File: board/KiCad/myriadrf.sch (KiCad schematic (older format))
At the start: 1 part, among them J1 FX10B_80S_8

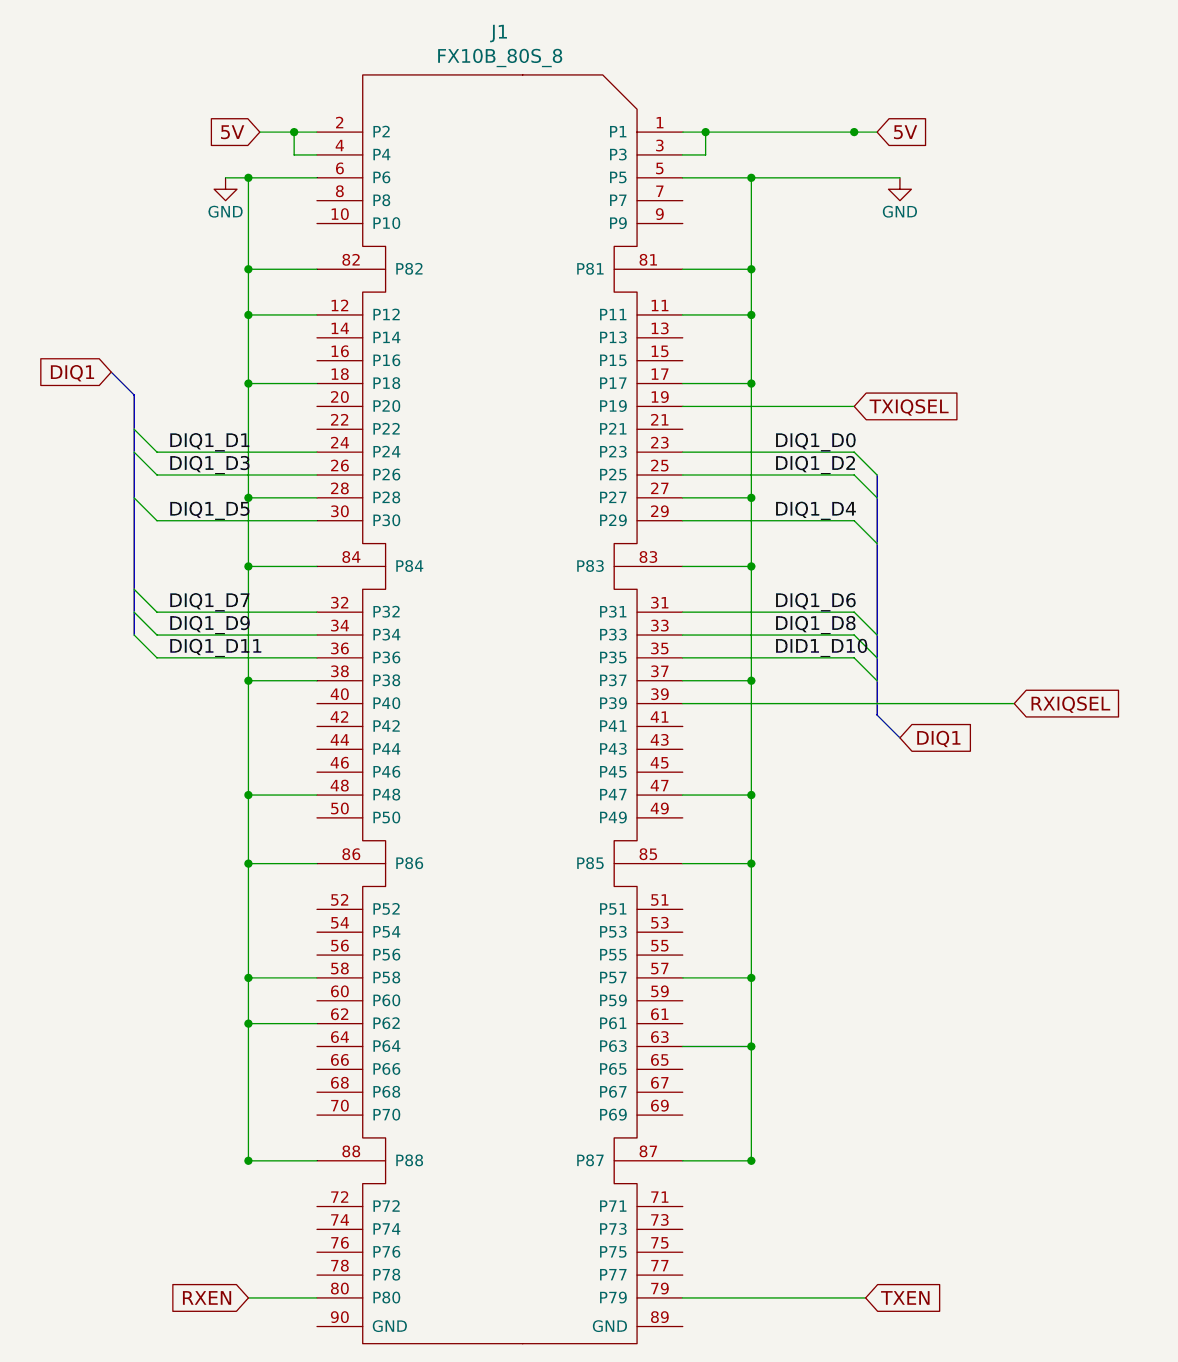
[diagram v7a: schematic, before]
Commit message: DIQ2 Bus added
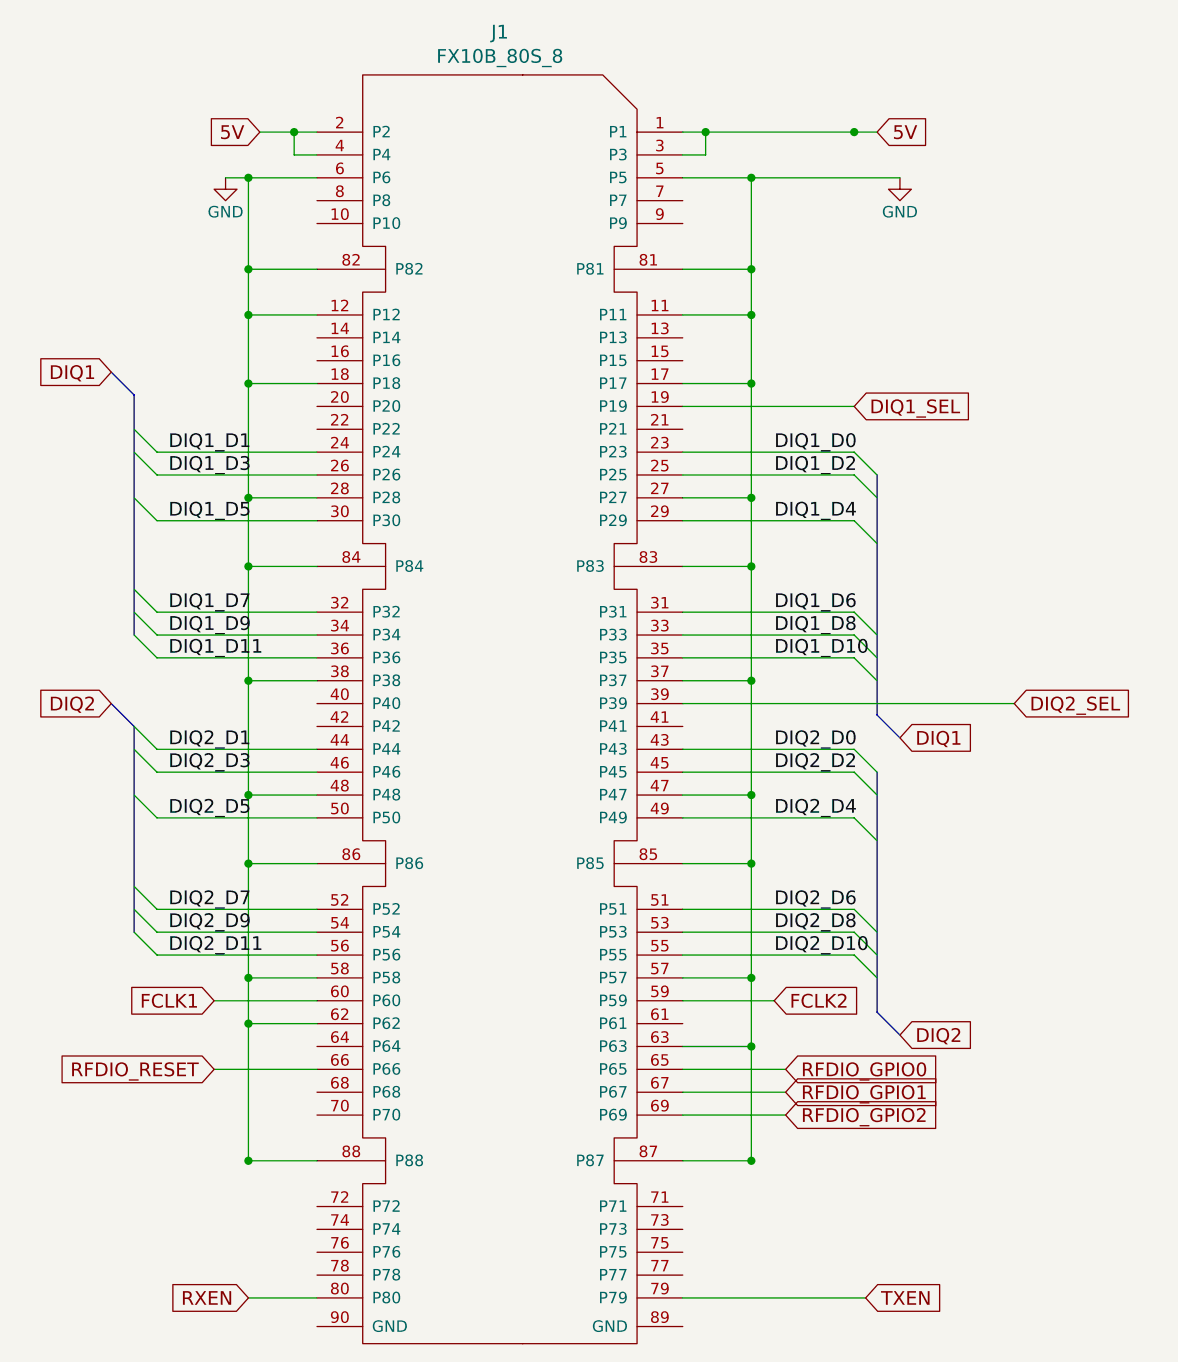
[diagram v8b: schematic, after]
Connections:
- net DIQ2_D0: now reaches J1.43 (P43)
- net DIQ2_D1: now reaches J1.44 (P44)
- net DIQ2_D2: now reaches J1.45 (P45)
- net DIQ2_D3: now reaches J1.46 (P46)
- net DIQ2_D4: now reaches J1.49 (P49)
- net DIQ2_D5: now reaches J1.50 (P50)
- net DIQ2_D6: now reaches J1.51 (P51)
- net DIQ2_D7: now reaches J1.52 (P52)
- net DIQ2_D8: now reaches J1.53 (P53)
- net DIQ2_D9: now reaches J1.54 (P54)
- net DIQ2_D10: now reaches J1.55 (P55)
- net DIQ2_D11: now reaches J1.56 (P56)
- net FCLK2: now reaches J1.59 (P59)
- net FCLK1: now reaches J1.60 (P60)
- net RFDIO_GPIO0: now reaches J1.65 (P65)
- net RFDIO_RESET: now reaches J1.66 (P66)
- net RFDIO_GPIO1: now reaches J1.67 (P67)
- net RFDIO_GPIO2: now reaches J1.69 (P69)
- net DID1_D10 renamed DIQ1_D10
- net RXIQSEL renamed DIQ2_SEL
- net TXIQSEL renamed DIQ1_SEL
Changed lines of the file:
@@
 DIQ1_D8
 Text Label 6800 3550 0    60   ~ 0
-DID1_D10
+DIQ1_D10
 Text Label 4150 2650 0    60   ~ 0
 DIQ1_D1
@@
 	6400 2450 7150 2450
 Text GLabel 7150 2450 2    60   Input ~ 0
-TXIQSEL
+DIQ1_SEL
 Wire Wire Line
 	6400 3750 7850 3750
 Text GLabel 7850 3750 2    60   Input ~ 0
-RXIQSEL
+DIQ2_SEL
 Wire Wire Line
 	4500 5750 4500 1450
@@
 Text GLabel 7200 6350 2    60   Input ~ 0
 TXEN
+Wire Bus Line
+	7250 4050 7250 5100
+Wire Wire Line
+	6400 3950 7150 3950
+Entry Wire Line
+	7150 3950 7250 4050
+Entry Wire Line
+	7150 4050 7250 4150
+Entry Wire Line
+	7150 4250 7250 4350
+Wire Wire Line
+	6400 4050 7150 4050
+Wire Wire Line
+	6400 4250 7150 4250
+Wire Wire Line
+	6400 4650 7150 4650
+Wire Wire Line
+	6400 4750 7150 4750
+Wire Wire Line
+	6400 4850 7150 4850
+Entry Wire Line
+	7150 4650 7250 4750
+Entry Wire Line
+	7150 4750 7250 4850
+Entry Wire Line
+	7150 4850 7250 4950
+Text Label 6800 3950 0    60   ~ 0
+DIQ2_D0
+Text Label 6800 4050 0    60   ~ 0
+DIQ2_D2
+Text Label 6800 4250 0    60   ~ 0
+DIQ2_D4
+Text Label 6800 4650 0    60   ~ 0
+DIQ2_D6
+Text Label 6800 4750 0    60   ~ 0
+DIQ2_D8
+Text Label 6800 4850 0    60   ~ 0
+DIQ2_D10
+Entry Bus Bus
+	7250 5100 7350 5200
+Text GLabel 7350 5200 2    60   Input ~ 0
+DIQ2
+Wire Wire Line
+	4800 3950 4100 3950
+Wire Wire Line
+	4800 4050 4100 4050
+Wire Wire Line
+	4800 4250 4100 4250
+Wire Wire Line
+	4800 4650 4100 4650
+Wire Wire Line
+	4800 4750 4100 4750
+Wire Wire Line
+	4800 4850 4100 4850
+Entry Wire Line
+	4000 3850 4100 3950
+Entry Wire Line
+	4000 3950 4100 4050
+Entry Wire Line
+	4000 4150 4100 4250
+Entry Wire Line
+	4000 4550 4100 4650
+Entry Wire Line
+	4000 4650 4100 4750
+Entry Wire Line
+	4000 4750 4100 4850
+Wire Bus Line
+	4000 4750 4000 3850
+Entry Bus Bus
+	3900 3750 4000 3850
+Text GLabel 3900 3750 0    60   Input ~ 0
+DIQ2
+Text Label 4150 3950 0    60   ~ 0
+DIQ2_D1
+Text Label 4150 4050 0    60   ~ 0
+DIQ2_D3
+Text Label 4150 4250 0    60   ~ 0
+DIQ2_D5
+Text Label 4150 4650 0    60   ~ 0
+DIQ2_D7
+Text Label 4150 4750 0    60   ~ 0
+DIQ2_D9
+Text Label 4150 4850 0    60   ~ 0
+DIQ2_D11
+Wire Wire Line
+	6400 5050 6800 5050
+Wire Wire Line
+	4800 5050 4350 5050
+Text GLabel 6800 5050 2    60   Input ~ 0
+FCLK2
+Text GLabel 4350 5050 0    60   Input ~ 0
+FCLK1
+Wire Wire Line
+	6400 5350 6850 5350
+Wire Wire Line
+	6400 5450 6850 5450
+Wire Wire Line
+	6400 5550 6850 5550
+Text GLabel 6850 5350 2    60   Input ~ 0
+RFDIO_GPIO0
+Text GLabel 6850 5450 2    60   Input ~ 0
+RFDIO_GPIO1
+Text GLabel 6850 5550 2    60   Input ~ 0
+RFDIO_GPIO2
+Wire Wire Line
+	4800 5350 4350 5350
+Text GLabel 4350 5350 0    60   Input ~ 0
+RFDIO_RESET
 $EndSCHEMATC
